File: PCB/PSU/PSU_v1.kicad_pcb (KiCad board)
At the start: 2 copper layers, 42.5 x 38.7 mm, 19 parts, among them J1 CONN_01X05, Q1 MPSA55, Q2 IRF630, U1 MC34063

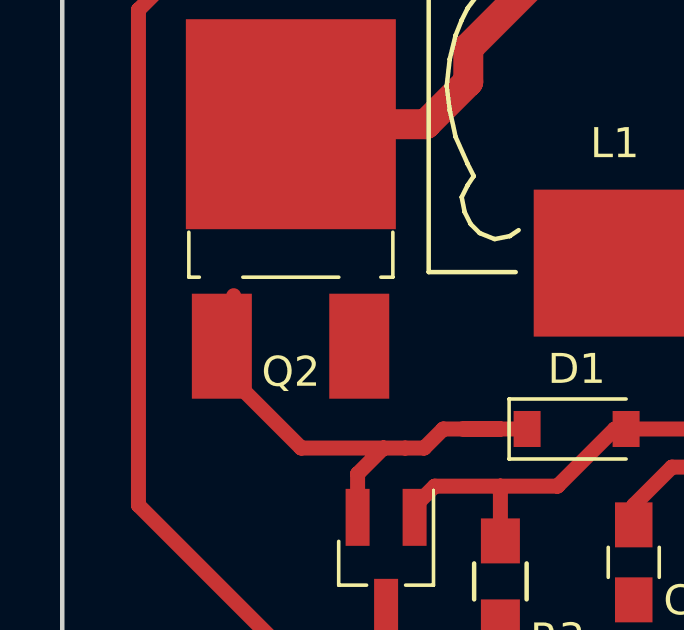
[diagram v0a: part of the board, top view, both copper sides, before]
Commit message: Microscopic trace delete
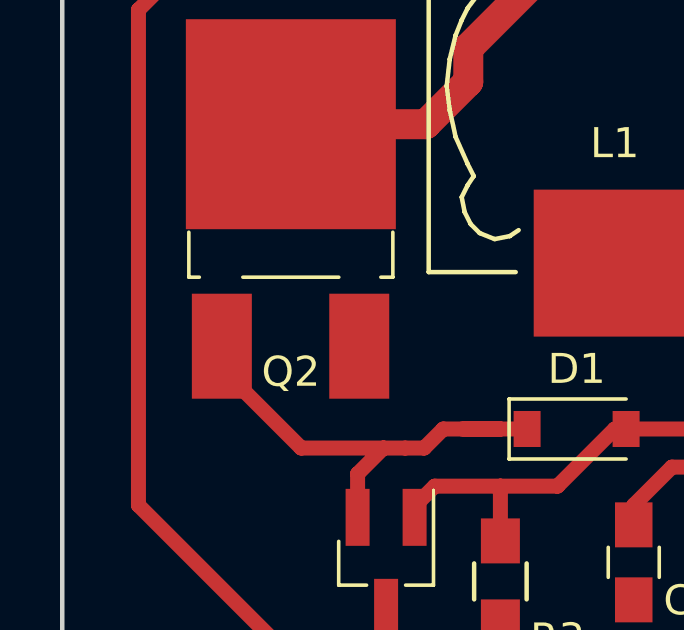
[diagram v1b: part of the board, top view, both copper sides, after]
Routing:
- net Net-(D1-Pad1): track 18.1 -> 16.8 mm
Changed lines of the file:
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@@
   (general
     (links 39)
-    (no_connects 0)
-    (area 121.209999 54.534999 163.905001 93.420001)
+    (no_connects 1)
+    (area 121.209999 54.534999 163.905001 94.085)
     (thickness 1.6)
     (drawings 7)
-    (tracks 111)
+    (tracks 110)
     (zones 0)
     (modules 19)
@@
     (pad_to_mask_clearance 0.2)
     (aux_axis_origin 0 0)
-    (visible_elements FFFFFF7F)
+    (visible_elements 7FFFFFFF)
     (pcbplotparams
-      (layerselection 0x00030_80000001)
+      (layerselection 0x00000_00000001)
       (usegerberextensions false)
-      (excludeedgelayer true)
+      (excludeedgelayer false)
       (linewidth 0.100000)
       (plotframeref false)
@@
       (hpglpendiameter 15)
       (hpglpenoverlay 2)
-      (psnegative false)
+      (psnegative true)
       (psa4output false)
       (plotreference true)
@@
       (padsonsilk false)
       (subtractmaskfromsilk false)
-      (outputformat 1)
+      (outputformat 4)
       (mirror false)
-      (drillshape 1)
+      (drillshape 0)
       (scaleselection 1)
       (outputdirectory ""))
@@
   (segment (start 133.985 84.455) (end 133.35 85.09) (width 0.5) (layer F.Cu) (net 6))
   (segment (start 126.605 81.695) (end 127 81.3) (width 0.5) (layer F.Cu) (net 6))
-  (segment (start 127 81.3) (end 127 80.01) (width 0.5) (layer F.Cu) (net 6))
   (segment (start 134.62 84.455) (end 135.89 84.455) (width 0.5) (layer F.Cu) (net 6))
   (segment (start 136.78 84.455) (end 135.89 84.455) (width 0.5) (layer F.Cu) (net 6))

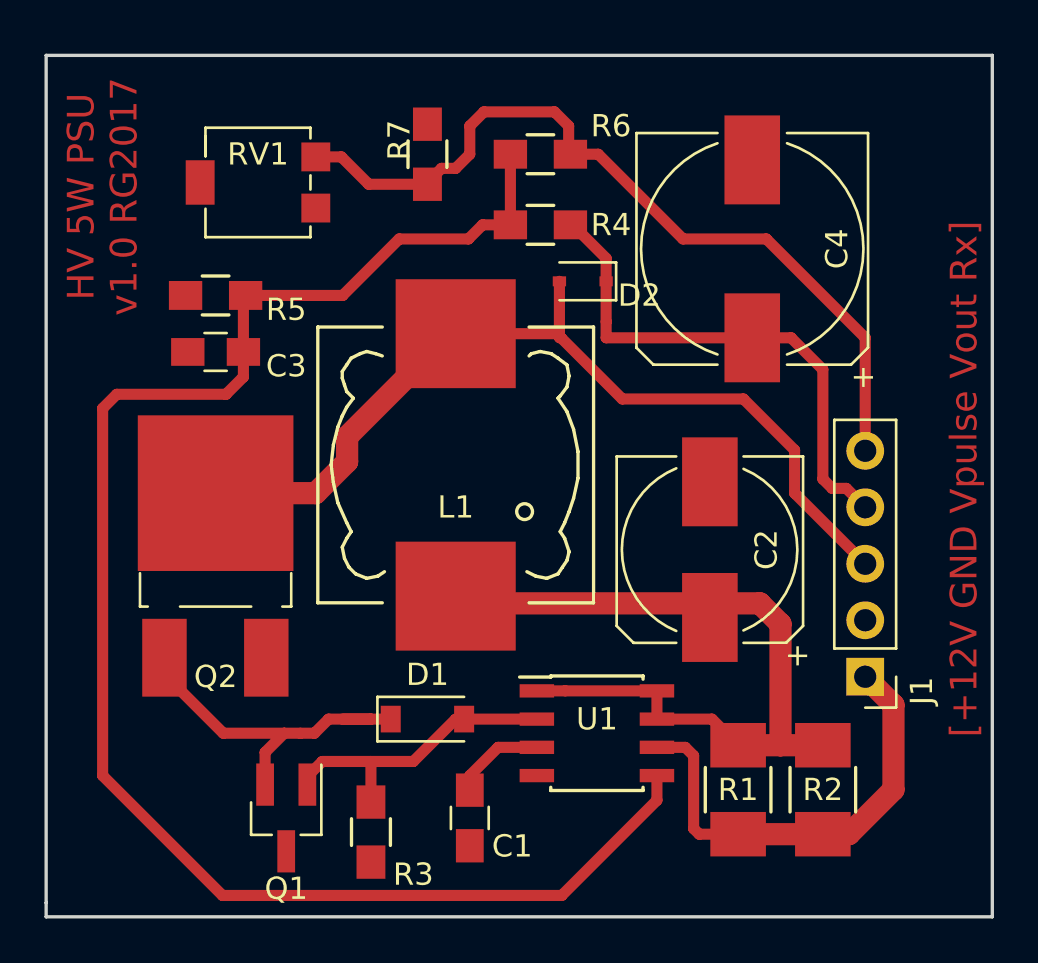
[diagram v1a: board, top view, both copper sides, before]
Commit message: Some tweaks to schematic and PCB based on laser etching prototyping
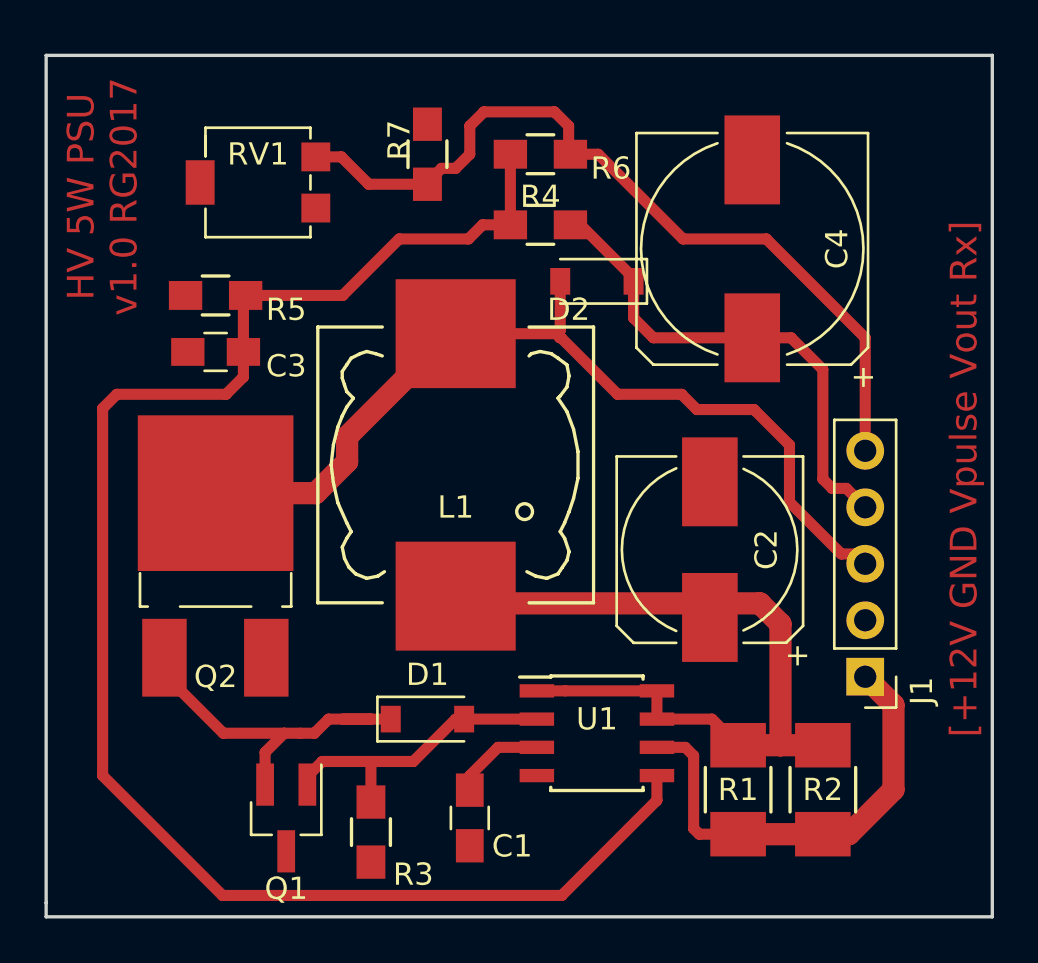
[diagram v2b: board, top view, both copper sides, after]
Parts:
- D2: footprint Diodes_SMD:D_SOD-323 -> Diodes_SMD:D_SOD-123
- moved D2 0.64 mm to (146.1, 64.8)
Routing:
- net /Vout: track 23.5 -> 22.5 mm
- net /Vpulse: track 40.7 -> 41.3 mm
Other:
- net class HV added: clearance 1, trace_width 0.5, via_dia 1, via_drill 0.5

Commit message: Edits to some component footprints due to component availability
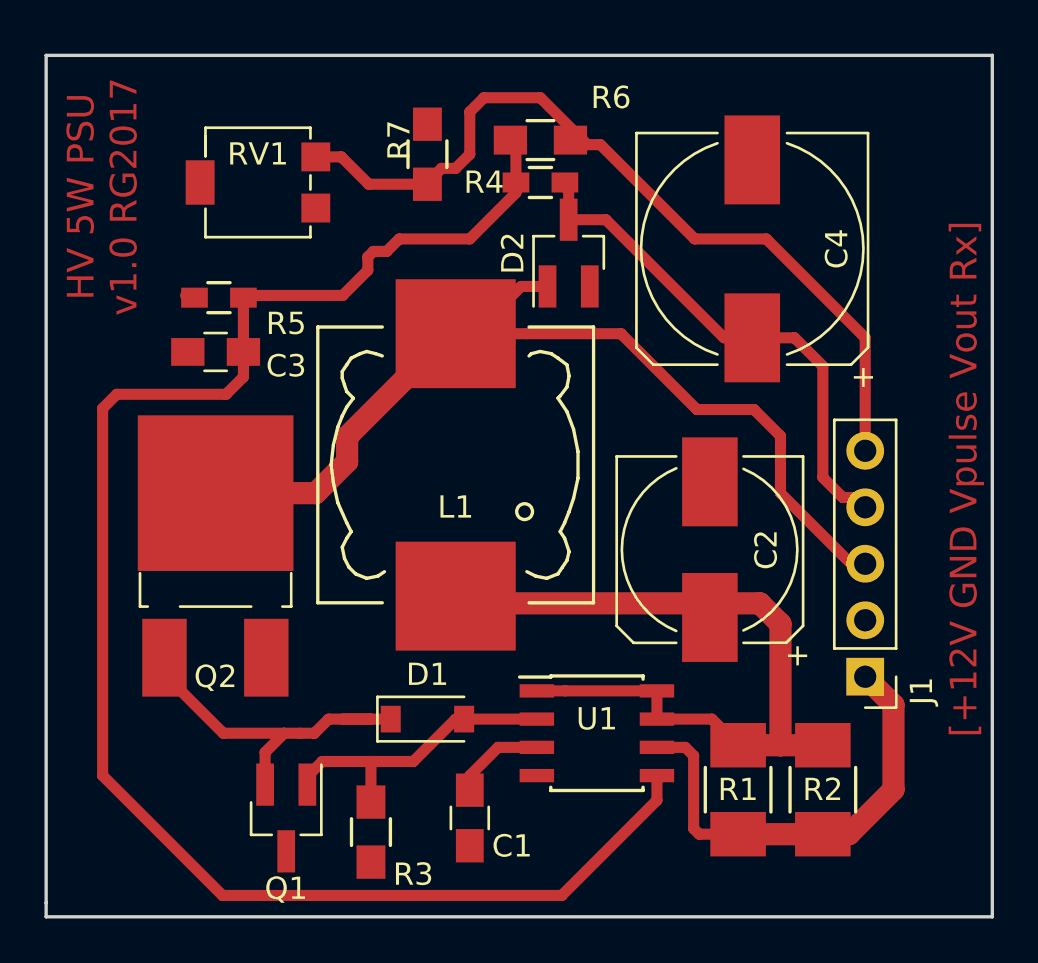
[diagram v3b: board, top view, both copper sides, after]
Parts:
- D2: value BAV21 -> BAS21; footprint Diodes_SMD:D_SOD-123 -> TO_SOT_Packages_SMD:SOT-23_Handsoldering
- R4, R5: footprint Resistors_SMD:R_0805_HandSoldering -> Resistors_SMD:R_0603_HandSoldering
- moved R4 1.90 mm to (143.5, 60.3)
- moved D2 1.80 mm to (144.8, 63.5), turned to 90 degrees
- moved R6 0.63 mm to (143.5, 58.4)
- moved R5 0.18 mm to (129.1, 65.5)
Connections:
- D2 pad 1: /Vout -> /Vpulse
- D2 pad 2: /Vpulse -> (no net)
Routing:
- net /Vpulse: track 41.3 -> 43.6 mm
- net /Vout: track 22.5 -> 23.2 mm
- added copper zone on F.Cu, net (none)
